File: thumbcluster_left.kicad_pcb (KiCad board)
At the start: 2 copper layers, 63.6 x 37.8 mm, 12 parts, among them J1 Conn_01x06_Female, J2 Conn_01x06_Female, SW1 SW_Push, SW2 SW_Push, SW3 SW_Push, SW4 SW_Push, SW5 SW_Push

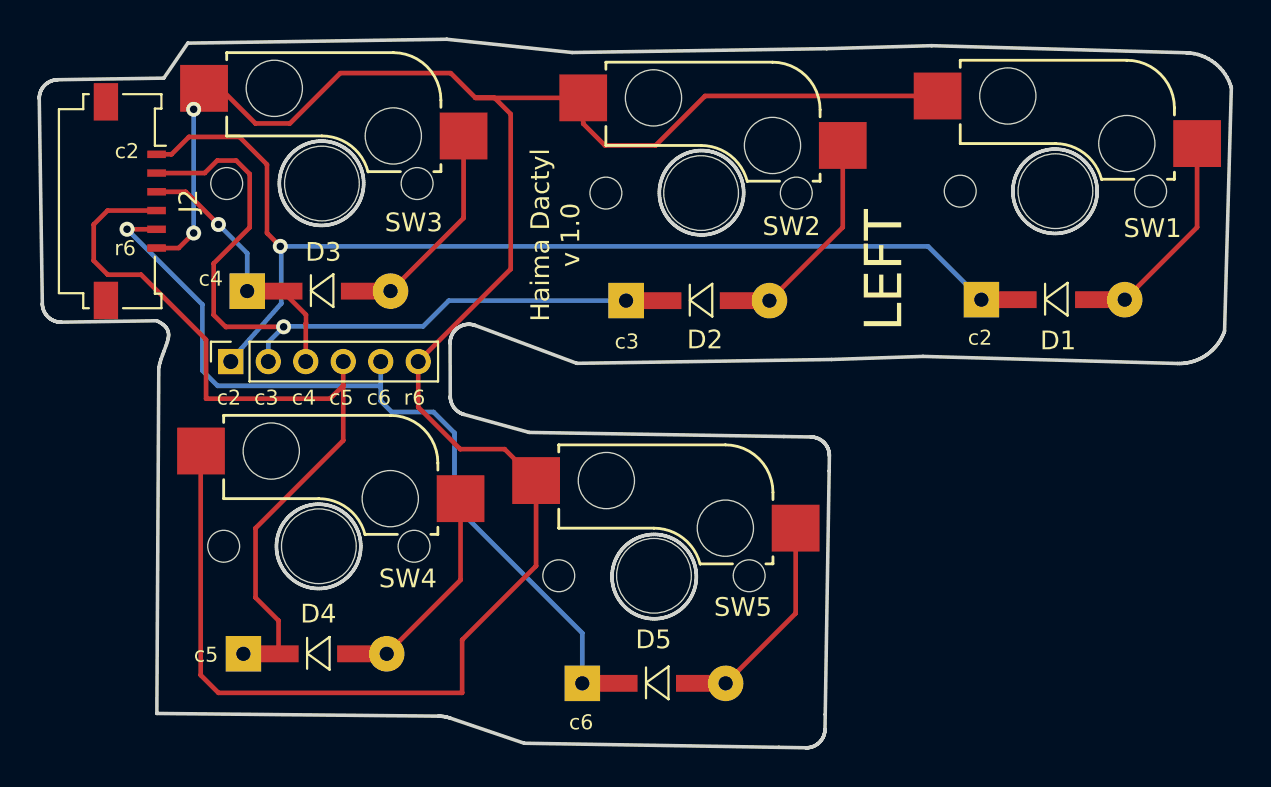
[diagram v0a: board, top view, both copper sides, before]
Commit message: Through hole switches
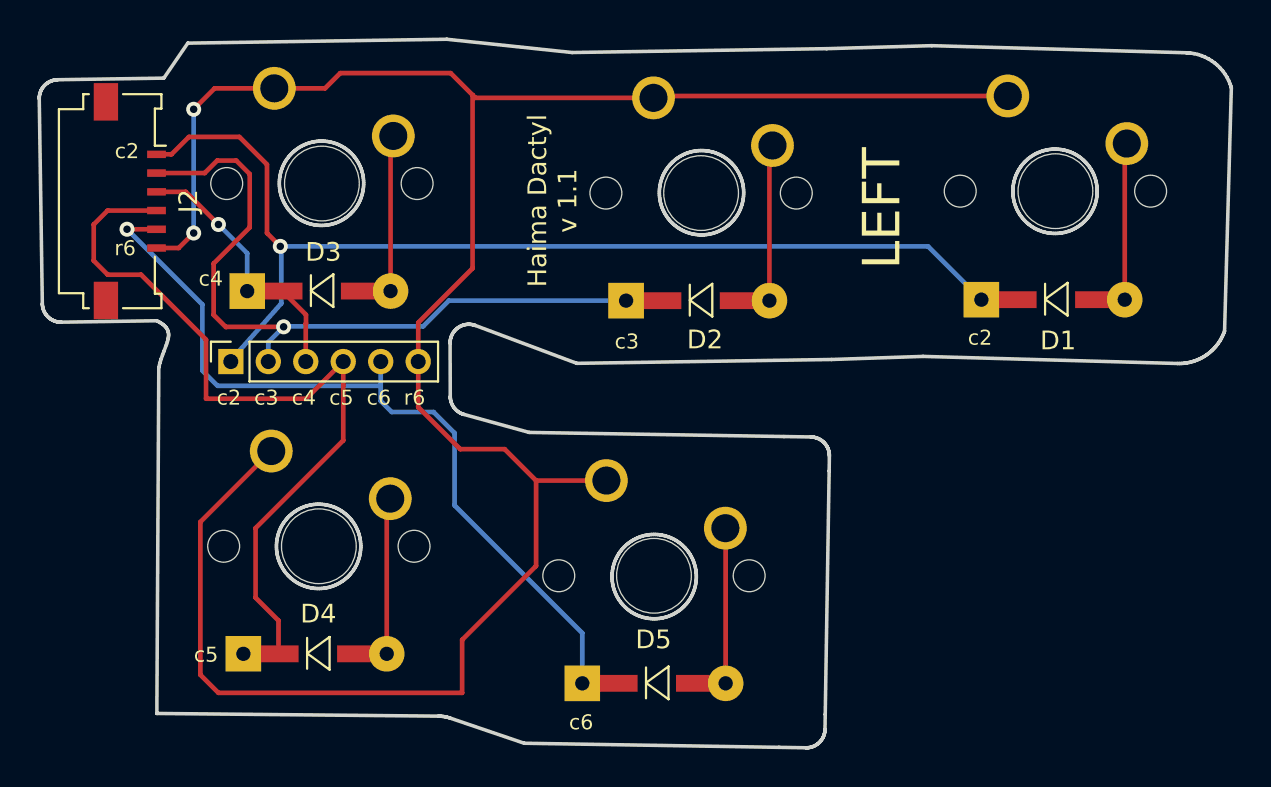
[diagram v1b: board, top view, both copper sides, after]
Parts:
- SW1, SW2, SW3, SW4, SW5: footprint keyswitches:Kailh_socket_MX -> keyswitches:SW_MX
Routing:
- net row6: track 120.6 -> 124.1 mm
- net Net-(D1-Pad2): track 9.93 -> 8.38 mm
- net Net-(D3-Pad2): track 9.89 -> 8.34 mm
- net Net-(D4-Pad2): track 9.91 -> 8.36 mm
- net Net-(D2-Pad2): track 9.90 -> 8.35 mm
- net Net-(D5-Pad2): track 9.83 -> 8.29 mm
- net col5: track 42.1 -> 42.7 mm
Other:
- board text added: "Haima Dactyl v 1.1"
- board text removed: "Haima Dactyl v 1.0"
